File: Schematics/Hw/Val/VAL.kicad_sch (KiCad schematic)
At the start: 2 parts

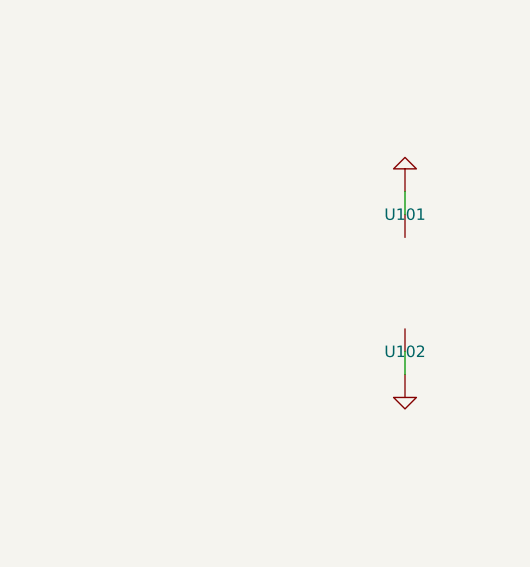
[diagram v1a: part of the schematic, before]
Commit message: (Re)apply values to the pull up/down symbols
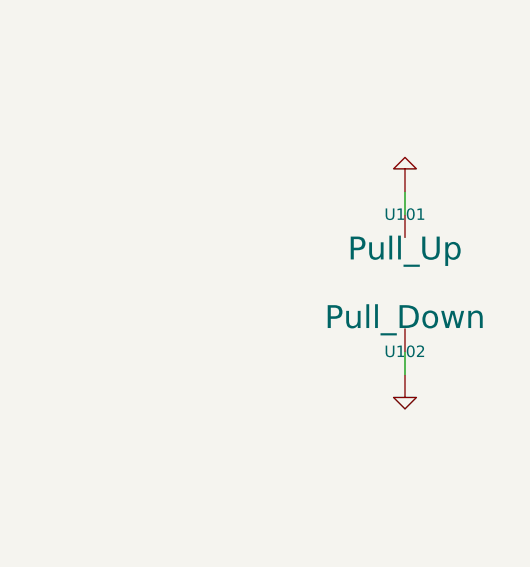
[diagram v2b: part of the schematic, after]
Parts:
- U101: value ~ -> Pull_Up
- U102: value ~ -> Pull_Down
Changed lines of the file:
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@@
 			)
 		)
-		(property "Value" "~"
+		(property "Value" "Pull_Down"
 			(at 566.42 255.27 0)
 			(effects
@@
 					(size 1.27 1.27)
 				)
+				(hide yes)
 			)
 		)
@@
 			)
 		)
-		(property "Value" "~"
+		(property "Value" "Pull_Up"
 			(at 566.42 247.65 0)
 			(effects
@@
 					(size 1.27 1.27)
 				)
+				(hide yes)
 			)
 		)
